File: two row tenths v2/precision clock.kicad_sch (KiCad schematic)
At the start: 66 parts, among them P1 USB_C_Plug_USB2.0, P2 USB_C_Plug_USB2.0, Q1 MMBT3904, U1 74AHCT125, Y1 Crystal

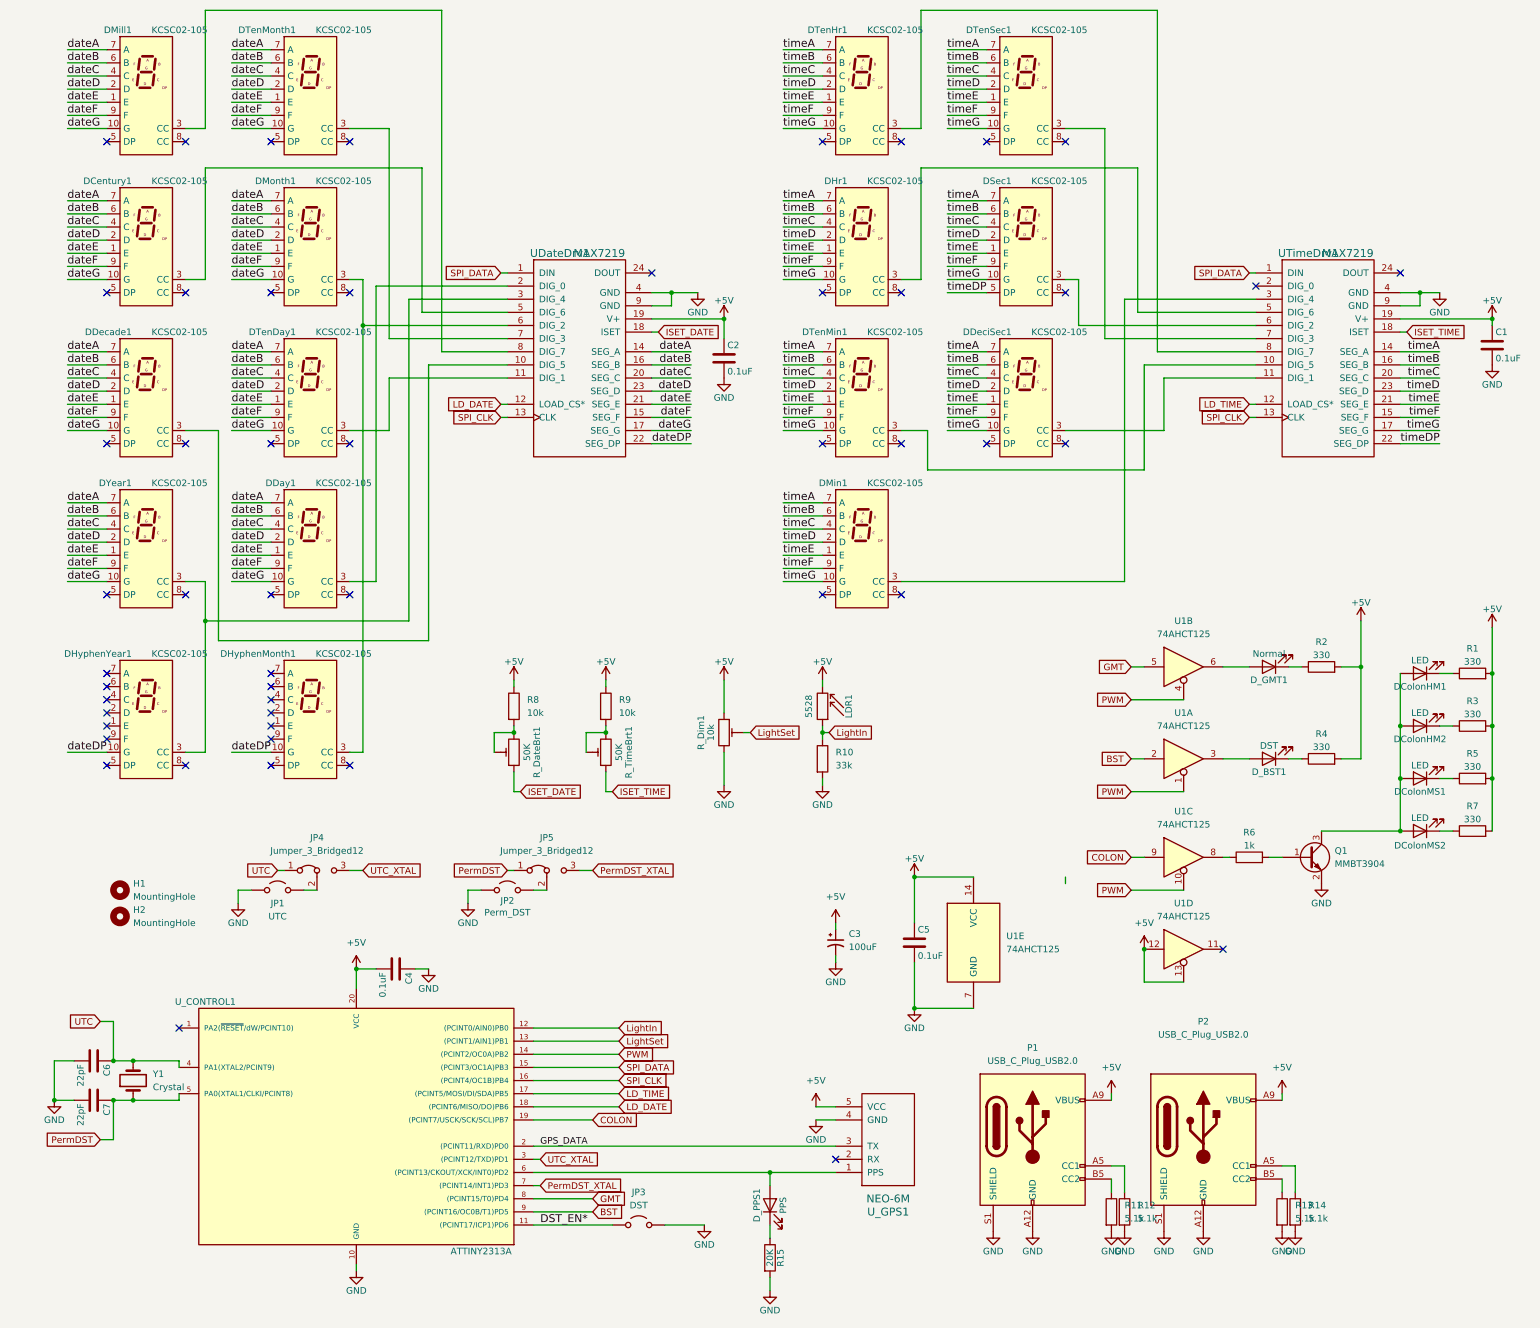
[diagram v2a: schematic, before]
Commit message: Add GPS model, sending to production.
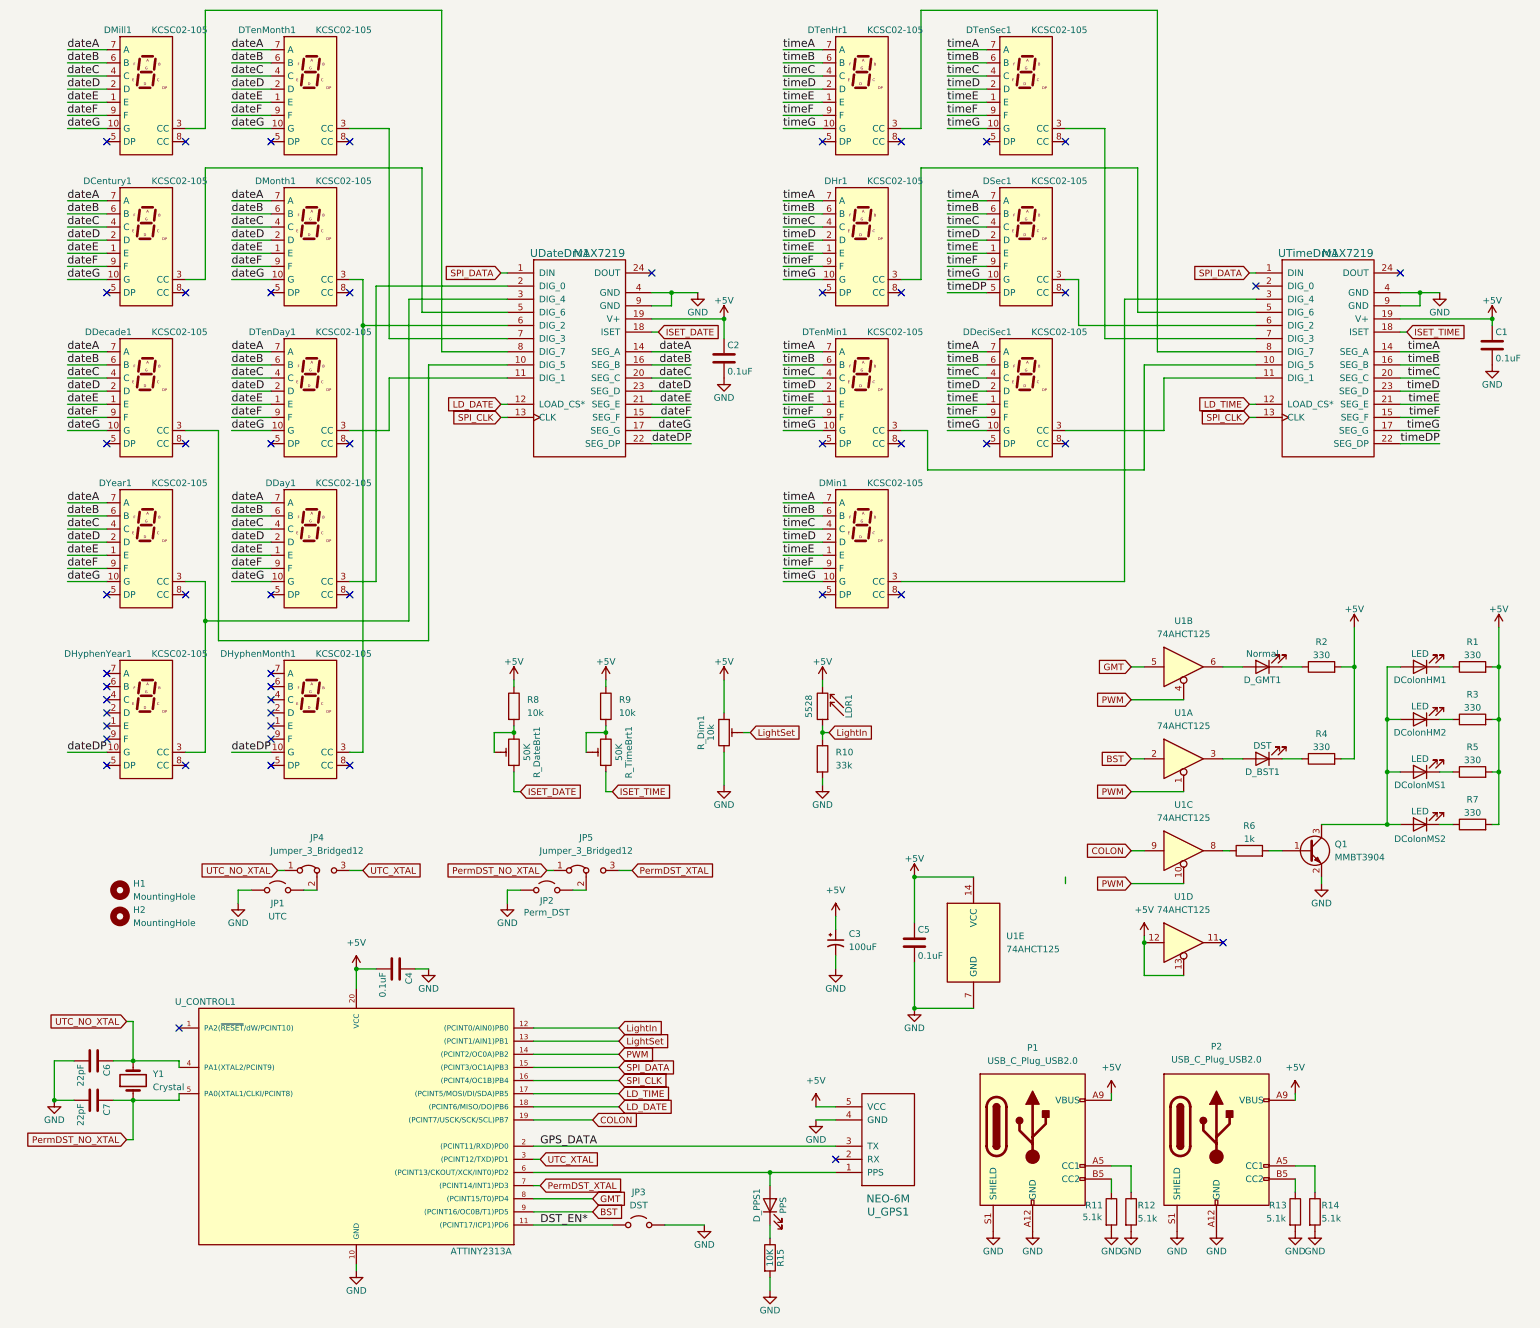
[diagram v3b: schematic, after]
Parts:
- JP4, JP5: footprint Jumper:SolderJumper-3_P1.3mm_Bridged2Bar12_Pad1.0x1.5mm -> Jumper:SolderJumper-3_P1.3mm_Bridged12_Pad1.0x1.5mm
- R15: value 20K -> 10K
- U_GPS1: footprint Connector_PinSocket_2.54mm:PinSocket_1x05_P2.54mm_Horizontal -> precision clock:ublox_GPS
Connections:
- net PermDST renamed PermDST_NO_XTAL
- net UTC renamed UTC_NO_XTAL
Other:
- moved on the sheet: DColonHM1, DColonHM2, DColonMS1, DColonMS2, D_BST1, D_GMT1, JP2, JP5, P2, Q1, R1, R12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

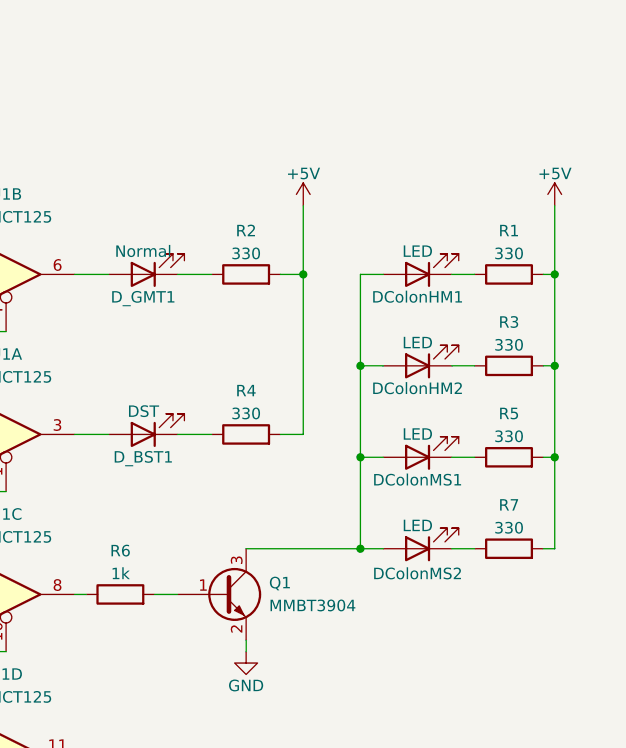
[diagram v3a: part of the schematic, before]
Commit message: Fix LED polarity, add STLs for antenna mounts
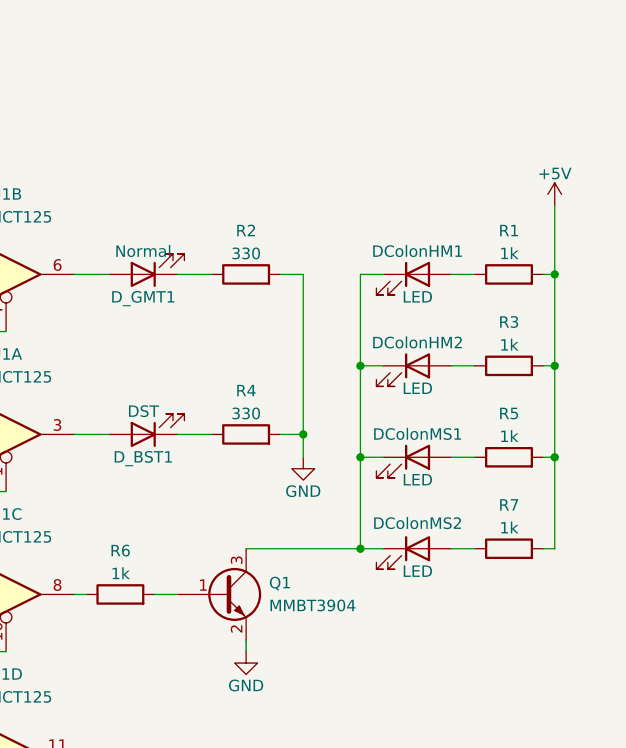
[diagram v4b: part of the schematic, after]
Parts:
- R1, R3, R5, R7: value 330 -> 1k
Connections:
- net +5V: no longer R2.2, R4.2
- net GND: now also R2.2, R4.2
- net at DColonHM2.1 (K): now also DColonHM1.1 (K), DColonMS1.1 (K), DColonMS2.1 (K), Q1.3 (C); no longer R3.1
- net at R5.1: now also DColonMS1.2 (A); no longer DColonMS1.1 (K)
- net at R7.1: now also DColonMS2.2 (A); no longer DColonMS2.1 (K)
- net at R1.1: now also DColonHM1.2 (A); no longer DColonHM1.1 (K)
- new net: DColonHM2.2 (A), R3.1
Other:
- moved on the sheet: DColonHM1, DColonHM2, DColonMS1, DColonMS2
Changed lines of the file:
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@@
 	)
 	(junction
-		(at 128.27 154.94)
+		(at 273.05 160.02)
 		(diameter 0)
 		(color 0 0 0 0)
 	)
 	(junction
-		(at 279.4 162.56)
+		(at 128.27 154.94)
 		(diameter 0)
 		(color 0 0 0 0)
 	)
 	(junction
-		(at 279.4 152.4)
+		(at 279.4 162.56)
 		(diameter 0)
 		(color 0 0 0 0)
 	)
 	(junction
-		(at 187.96 208.28)
+		(at 279.4 152.4)
 		(diameter 0)
 		(color 0 0 0 0)
 	)
 	(junction
-		(at 273.05 142.24)
+		(at 187.96 208.28)
 		(diameter 0)
 		(color 0 0 0 0)
@@
 	(wire
 		(pts
-			(xy 273.05 142.24) (xy 273.05 134.62)
-		)
-		(stroke
-			(width 0)
-			(type default)
-		)
-	)
-	(wire
-		(pts
 			(xy 137.16 91.44) (xy 144.78 91.44)
 		)
@@
 	(wire
 		(pts
+			(xy 273.05 160.02) (xy 273.05 162.56)
+		)
+		(stroke
+			(width 0)
+			(type default)
+		)
+	)
+	(wire
+		(pts
 			(xy 172.72 234.95) (xy 114.3 234.95)
 		)
@@
 	(symbol
 		(lib_id "Device:LED")
-		(at 285.75 152.4 180)
+		(at 285.75 152.4 0)
 		(unit 1)
 		(exclude_from_sim no)
@@
 		(dnp no)
 		(property "Reference" "DColonHM2"
-			(at 285.75 154.94 0)
+			(at 285.75 149.86 0)
 			(effects
 				(font
@@
 		)
 		(property "Value" "LED"
-			(at 285.75 149.86 0)
+			(at 285.75 154.94 0)
 			(effects
 				(font
@@
 	(symbol
 		(lib_id "Device:LED")
-		(at 285.75 162.56 180)
+		(at 285.75 162.56 0)
 		(unit 1)
 		(exclude_from_sim no)
@@
 		(dnp no)
 		(property "Reference" "DColonMS1"
-			(at 285.75 165.1 0)
+			(at 285.75 160.02 0)
 			(effects
 				(font
@@
 		)
 		(property "Value" "LED"
-			(at 285.75 160.02 0)
+			(at 285.75 165.1 0)
 			(effects
 				(font
@@
 	(symbol
 		(lib_id "Device:LED")
-		(at 285.75 172.72 180)
+		(at 285.75 172.72 0)
 		(unit 1)
 		(exclude_from_sim no)
@@
 		(dnp no)
 		(property "Reference" "DColonMS2"
-			(at 285.75 175.514 0)
+			(at 285.75 169.926 0)
 			(effects
 				(font
@@
 		)
 		(property "Value" "LED"
-			(at 285.75 170.18 0)
+			(at 285.75 175.26 0)
 			(effects
 				(font
@@
 	(symbol
 		(lib_id "Device:LED")
-		(at 285.75 142.24 180)
+		(at 285.75 142.24 0)
 		(unit 1)
 		(exclude_from_sim no)
@@
 		(dnp no)
 		(property "Reference" "DColonHM1"
-			(at 285.75 144.78 0)
+			(at 285.75 139.7 0)
 			(effects
 				(font
@@
 		)
 		(property "Value" "LED"
-			(at 285.75 139.7 0)
+			(at 285.75 144.78 0)
 			(effects
 				(font
@@
 			)
 		)
-		(property "Value" "330"
+		(property "Value" "1k"
 			(at 295.91 139.954 90)
 			(effects
@@
 	)
 	(symbol
+		(lib_id "power:GND")
+		(at 273.05 162.56 0)
+		(unit 1)
+		(exclude_from_sim no)
+		(in_bom yes)
+		(on_board yes)
+		(dnp no)
+		(property "Reference" "#PWR041"
+			(at 273.05 168.91 0)
+			(effects
+				(font
+					(size 1.27 1.27)
+				)
+				(hide yes)
+			)
+		)
+		(property "Value" "GND"
+			(at 273.05 166.37 0)
+			(effects
+				(font
+					(size 1.27 1.27)
+				)
+			)
+		)
+		(property "Footprint" ""
+			(at 273.05 162.56 0)
+			(effects
+				(font
+					(size 1.27 1.27)
+				)
+				(hide yes)
+			)
+		)
+		(property "Datasheet" ""
+			(at 273.05 162.56 0)
+			(effects
+				(font
+					(size 1.27 1.27)
+				)
+				(hide yes)
+			)
+		)
+		(property "Description" "Power symbol creates a global label with name \"GND\" , ground"
+			(at 273.05 162.56 0)
+			(effects
+				(font
+					(size 1.27 1.27)
+				)
+				(hide yes)
+			)
+		)
+		(pin "1"
+		)
+		(instances
+			(project "precision clock"
+				(path "/a352d3ae-caca-4fe6-94e2-4912021cb238"
+					(reference "#PWR041")
+					(unit 1)
+				)
+			)
+		)
+	)
+	(symbol
 		(lib_id "Device:LED")
 		(at 255.27 142.24 180)
@@
 			)
 		)
-		(property "Value" "330"
+		(property "Value" "1k"
 			(at 295.91 160.274 90)
 			(effects
@@
 	)
 	(symbol
-		(lib_id "power:VCC")
-		(at 273.05 134.62 0)
-		(unit 1)
-		(exclude_from_sim no)
-		(in_bom yes)
-		(on_board yes)
-		(dnp no)
-		(property "Reference" "#PWR08"
-			(at 273.05 138.43 0)
-			(effects
-				(font
-					(size 1.27 1.27)
-				)
-				(hide yes)
-			)
-		)
-		(property "Value" "+5V"
-			(at 273.05 131.064 0)
-			(effects
-				(font
-					(size 1.27 1.27)
-				)
-			)
-		)
-		(property "Footprint" ""
-			(at 273.05 134.62 0)
-			(effects
-				(font
-					(size 1.27 1.27)
-				)
-				(hide yes)
-			)
-		)
-		(property "Datasheet" ""
-			(at 273.05 134.62 0)
-			(effects
-				(font
-					(size 1.27 1.27)
-				)
-				(hide yes)
-			)
-		)
-		(property "Description" "Power symbol creates a global label with name \"VCC\""
-			(at 273.05 134.62 0)
-			(effects
-				(font
-					(size 1.27 1.27)
-				)
-				(hide yes)
-			)
-		)
-		(pin "1"
-		)
-		(instances
-			(project "precision clock"
-				(path "/a352d3ae-caca-4fe6-94e2-4912021cb238"
-					(reference "#PWR08")
-					(unit 1)
-				)
-			)
-		)
-	)
-	(symbol
 		(lib_id "Device:R")
 		(at 170.18 160.02 0)
@@
 			)
 		)
-		(property "Value" "330"
+		(property "Value" "1k"
 			(at 295.91 150.114 90)
 			(effects
@@
 			)
 		)
-		(property "Value" "330"
+		(property "Value" "1k"
 			(at 295.91 170.434 90)
 			(effects
